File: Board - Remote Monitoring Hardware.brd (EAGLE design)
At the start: 92.7 x 49.8 mm, 49 parts, among them IC1 MSP430G2 Socket, IC2 TPS77301, IC3 Xbee S3 Socket, IC4 MAX31855T, J5 Mono 2.5mm, Q1 MC-405

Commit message: board and schematics update May 25 2017
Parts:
- removed J5: Mono 2.5mm, con-lumberg:1501_05
- added J5A: (no value), SparkFun-Connectors:SCREWTERMINAL-3.5MM-2
- added J5B: PCC-SMP, custom parts:PCC-SMP
- C7: value 1uF/6.3V -> 10uF
- C8: value 100uF -> 100nF
- moved IC4 54.0 mm to (55.2, 35.6), turned to 0 degrees
- moved R8 42.3 mm to (47.0, 37.5), turned to 0 degrees
- moved S3 40.4 mm to (5.71, 12.7), turned to 180 degrees
- moved R9 40.0 mm to (40.0, 37.5), turned to 0 degrees
- moved J7 35.1 mm to (5.08, 25.4), turned to 270 degrees
- moved L1 34.5 mm to (51.4, 23.5)
- moved C9 33.8 mm to (54.0, 26.7), turned to 0 degrees
- moved L2 33.2 mm to (56.5, 23.5)
- moved J2 32.4 mm to (30.5, 20.3)
- moved C11 29.3 mm to (34.9, 37.5), turned to 0 degrees
- moved C10 28.7 mm to (29.8, 37.5), turned to 0 degrees
- moved C1 25.1 mm to (12.7, 4.45), turned to 180 degrees
- moved C2 24.8 mm to (17.8, 4.45), turned to 180 degrees
- moved D2 24.0 mm to (27.9, 3.81)
- moved R4 19.3 mm to (40.0, 20.3)
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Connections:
- removed net DIN: J6.2
- removed net DOUT: J6.3
- net N$14: now also J5A.2, J5B.T-; no longer J5.2, J5.3
- net N$15: now also J5A.1, J5B.T+; no longer J5.1
- net P1.1: now also J6.3
- net P1.2: now also J6.2
- net VCC: now also S2.1; no longer S2.2
- net VCC_XBEE: now also S2.2; no longer S2.1
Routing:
- net VCC: track 0.00 -> 132.9 mm, vias 0 -> 2
- net P1.2: track 0.00 -> 113.9 mm
- net P1.1: track 0.00 -> 110.6 mm
- net VCC_XBEE: track 0.00 -> 110.3 mm
- net 1: track 0.00 -> 109.8 mm, vias 0 -> 2
- net RST/SBWTDIO: track 0.00 -> 94.6 mm, vias 0 -> 2
- net 2: track 0.00 -> 83.2 mm, vias 0 -> 4
- net P1.3: track 0.00 -> 55.7 mm, vias 0 -> 2
- net +3.3VIN1: track 0.00 -> 46.2 mm
- net XOUTR: track 0.00 -> 43.5 mm
- net N$15: track 0.00 -> 41.2 mm
- net P1.6: track 0.00 -> 40.7 mm, vias 0 -> 2
- net N$14: track 0.00 -> 39.6 mm
- net +3.3VIN2: track 0.00 -> 35.8 mm
- net XINR: track 0.00 -> 35.1 mm
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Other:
- board size 92.7 x 49.8 mm -> 92.7 x 56.2 mm
- board text added: "(C) 2017 Vincent Aulia"
- board text added: "MSP430 Target Board Socket Mark I"
- board text removed: "MSP430G2 Target Socket Mark I"

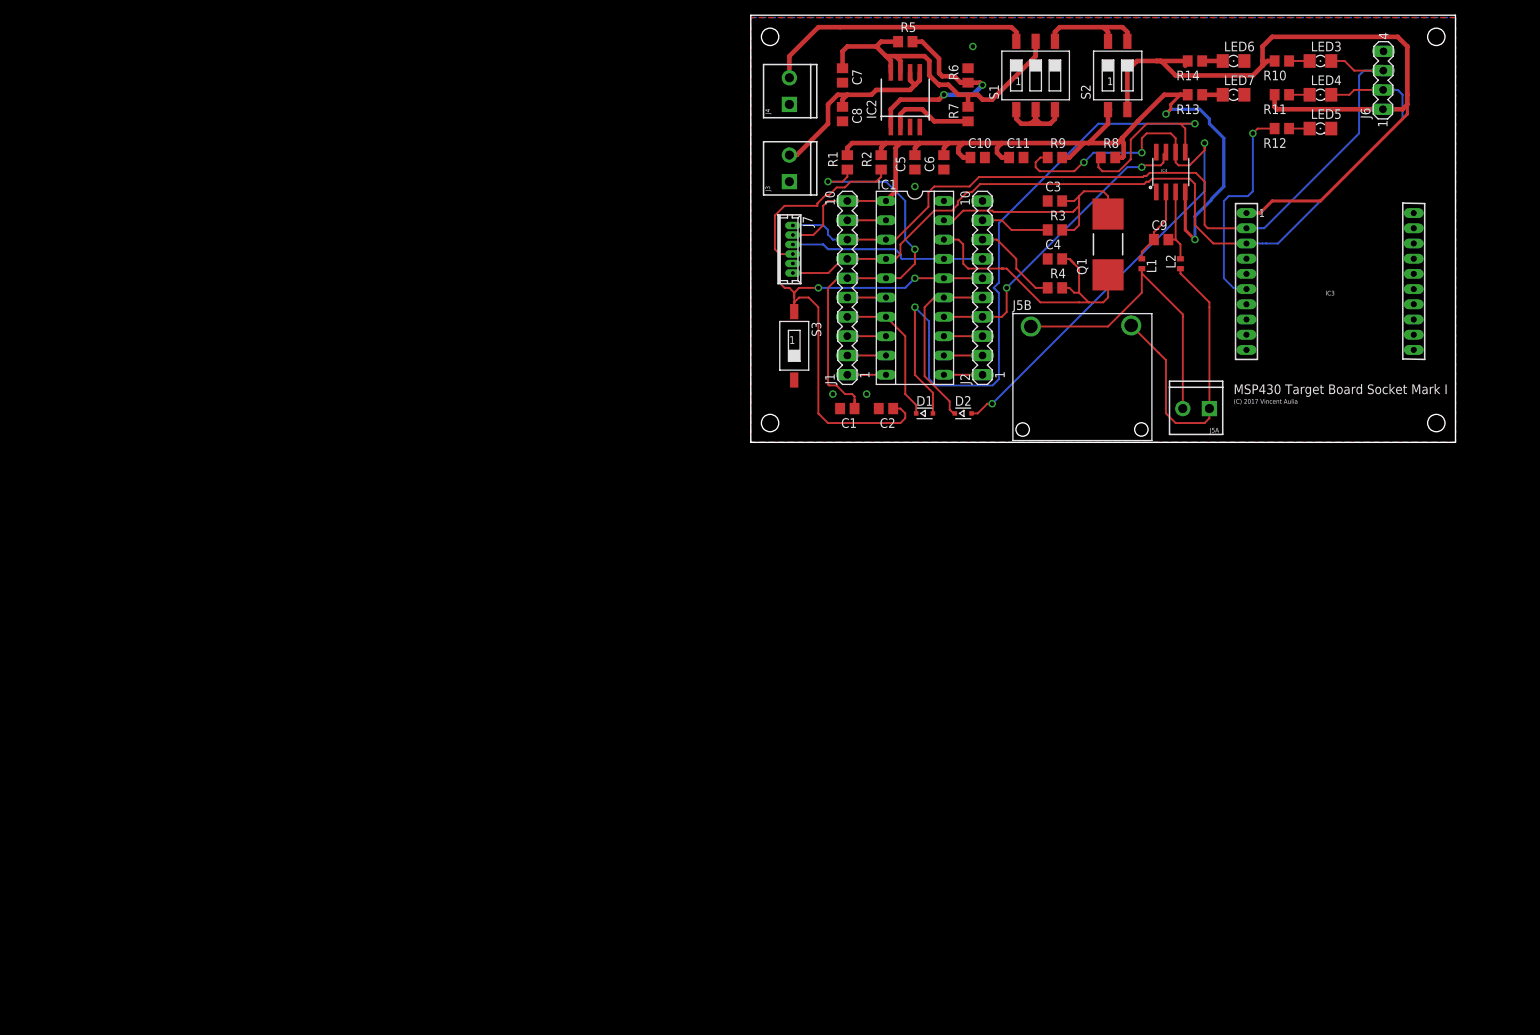
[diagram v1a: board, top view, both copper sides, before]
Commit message: Added BOM + brd & sch changes Aug 28 2017
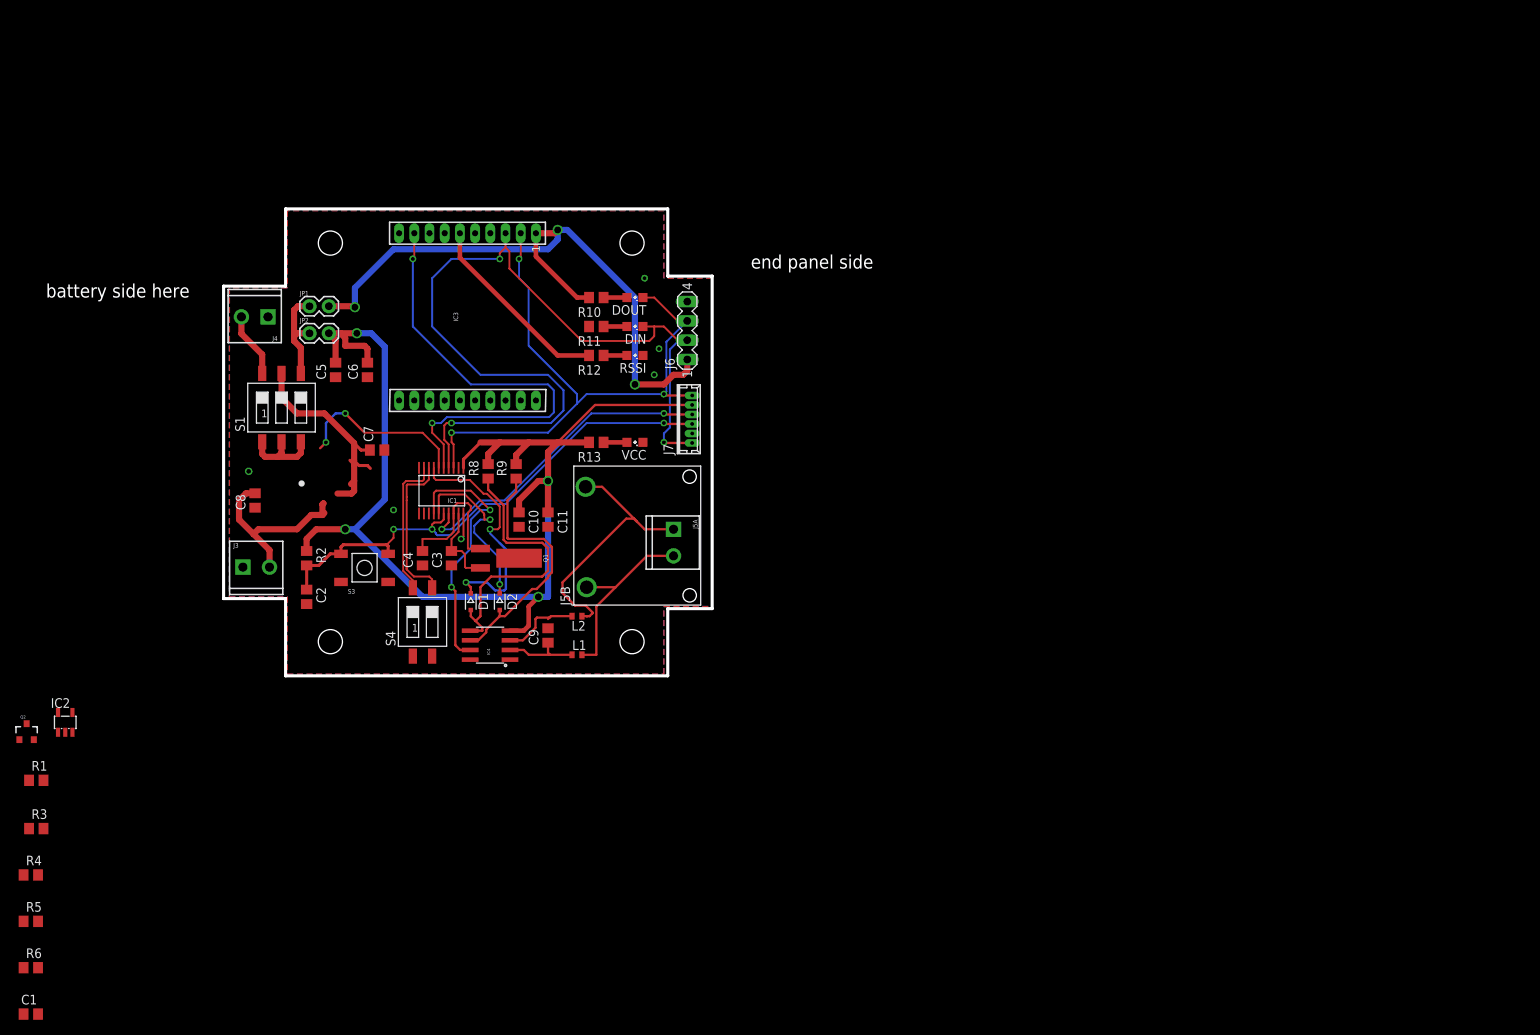
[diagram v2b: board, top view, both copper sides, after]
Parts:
- removed J1, J2: (no value), con-lstb:MA10-1
- removed LED3, LED4, LED6, LED7: Green, eagle-ltspice:LED_1206
- removed LED5: Red, eagle-ltspice:LED_1206
- removed R14: 1k, eagle-ltspice:R0805
- removed R7: 250k, eagle-ltspice:R0805
- removed S2: (no value), smd-special:SMS-002
- added DIN: LED4, led:SML0805
- added DOUT: LED3, led:SML0805
- added JP1, JP2: (no value), SparkFun-Retired:1X02
- added Q2: DMP3099L-7, User-Submitted:SOT23-3
- added RSSI: LED5, led:SML0805
- added S4: (no value), smd-special:SMS-002
- added VCC: LED7, led:SML0805
- C1: value 100nF -> 0.1uF
- C7: value 10uF -> 4.7uF
- C8: value 100nF -> 1uF
- IC1: value MSP430G2 Socket -> MSP430G2553; device ic-package:SOCKET-20 -> custom parts:MSP430G2553IPW20
- IC2: value TPS77301 -> TPS77001; device texas:SOP-08 -> texas:SOT23-DBV
- Q1: value MC-405 -> 32.768kHz; device crystal:MC-405 -> SparkFun-Clocks:CRYSTAL-SMD-2X6-CYL
- R1: value 47k -> 287k
- R3: value 0R -> 169k
- R4: value 0R -> 172k
- R5: value 53.8k -> 100k
- R6: value 30.1k -> 10k
- S3: value (none) -> SMD-PUSHBTN-SWTVER1; device smd-special:SMS-001 -> custom parts:KPT-1187B
- moved R6 170.2 mm to (-94.7, -69.1), turned to 0 degrees
- moved R5 163.1 mm to (-94.7, -63.0)
- moved R3 155.4 mm to (-94.0, -50.8)
- moved R4 155.3 mm to (-94.7, -56.9)
- moved IC2 137.5 mm to (-90.2, -36.8)
- moved R1 134.1 mm to (-94.0, -44.5), turned to 0 degrees
- moved C1 133.7 mm to (-94.7, -75.2), turned to 0 degrees
- moved IC3 124.6 mm to (-48.3, 16.5), turned to 270 degrees
- moved IC4 109.0 mm to (-34.3, -26.7), turned to 90 degrees
- moved S1 108.4 mm to (-61.7, 4.57)
- moved J6 97.3 mm to (-8.36, 14.7), turned to 90 degrees
- moved C9 96.0 mm to (-26.7, -25.4), turned to 90 degrees
- moved R10 95.4 mm to (-20.3, 19.1)
- moved R11 95.2 mm to (-20.3, 15.2)
- moved R12 95.0 mm to (-20.3, 11.4)
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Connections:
- removed net DTR: IC3.9
- removed net N$18: LED6.A, R14.1
- removed net XIN: J2.9, R3.1
- removed net XOUT: J2.8, R4.1
- new net N$3: Q2.3, R4.2
- net +3.3VIN1: now also IC2.5, R1.2; no longer IC2.7, IC2.8, R5.1, R7.2
- net +9VIN: now also IC2.1, Q2.2, R6.2; no longer IC2.5, IC2.6
- net GND: now also IC2.2, R3.1, R5.1, RSSI.C, S3.3, S3.4, S4.1, S4.2, VCC.C; no longer C1.2, IC2.4, J2.10, LED5.C, LED6.C, LED7.C, R6.2, S3.2
- net N$10: now also DIN.A; no longer LED4.A
- net N$11: now also RSSI.A; no longer LED5.A
- net N$16: now also JP1.1, JP2.1; no longer S2.3, S2.4
- net N$17: now also VCC.A; no longer LED7.A
- net N$2: now also C1.2, Q2.1; no longer IC2.1, R5.2
- net N$4: now also DOUT.A; no longer LED3.A
- net N$5: now also IC2.4, R1.1, R3.2; no longer IC2.2, R7.1
- net P1.0: no longer J1.9
- net P1.1: now also DOUT.C; no longer J1.8, LED3.C
- net P1.2: now also DIN.C; no longer J1.7, LED4.C
- net P1.3: now also IC3.9; no longer C1.1, J1.6, R1.1
- net P1.4: now also R4.1, R5.2; no longer J1.5
- net P1.5: no longer J1.4
- net P1.6: no longer J2.4
- net P1.7: no longer J2.5
- net P2.0: now also S4.3; no longer J1.3
- net P2.1: now also S4.4; no longer J1.2
- net P2.2: now also C1.1; no longer J1.1
- net P2.3: no longer J2.1
- net P2.4: no longer J2.2
- net P2.5: no longer J2.3
- net RST/SBWTDIO: now also S3.2; no longer J2.6
- net TEST/SBWTCK: no longer J2.7
- net VCC: now also JP2.2; no longer J1.10, R1.2, S2.1
- net VCC_XBEE: now also JP1.2; no longer R14.2, S2.2
- net XINR: now also Q1.X2; no longer Q1.2, R3.2
- net XOUTR: now also Q1.X1; no longer Q1.1, R4.2
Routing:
- net 1: track 109.8 -> 37.6 mm, vias 2 -> 0
- net 2: track 83.2 -> 33.5 mm, vias 4 -> 0
- net VCC: track 132.9 -> 166.2 mm, vias 2 -> 4
- net N$2: track 28.4 -> 0.00 mm, vias 2 -> 0
- net P1.1: track 110.6 -> 82.3 mm, vias 0 -> 3
- net +3.3VIN2: track 35.8 -> 8.58 mm
- net RST/SBWTDIO: track 94.6 -> 68.1 mm, vias 2 -> 3
- net XINR: track 35.1 -> 11.0 mm
- net VCC_XBEE: track 110.3 -> 86.3 mm, vias 0 -> 3
- net XOUTR: track 43.5 -> 19.7 mm
- net P1.4: track 5.08 -> 23.4 mm, vias 0 -> 2
- net +3.3VIN1: track 46.2 -> 30.2 mm
- net P2.0: track 5.08 -> 21.0 mm
- net TEST/SBWTCK: track 26.0 -> 41.8 mm, vias 0 -> 2
- net N$14: track 39.6 -> 25.0 mm
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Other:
- board size 92.7 x 56.2 mm -> 64.3 x 61.4 mm
- board text added: "battery side here"
- board text added: "end panel side"
- board text removed: "(C) 2017 Vincent Aulia"
- board text removed: "MSP430 Target Board Socket Mark I"

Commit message: brd & sch changes Sept 12 2017
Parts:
- moved C1 86.8 mm to (-46.8, -2.78), turned to 180 degrees
- moved R5 82.1 mm to (-44.0, 1.48), turned to 270 degrees
- moved R6 77.8 mm to (-48.7, -6.33), turned to 180 degrees
- moved R4 75.6 mm to (-46.6, 1.49), turned to 90 degrees
- moved Q2 58.2 mm to (-51.1, -0.14), turned to 270 degrees
- moved R3 57.2 mm to (-57.1, -6.99), turned to 90 degrees
- moved R1 55.7 mm to (-54.6, -5.08), turned to 90 degrees
- moved IC2 42.6 mm to (-61.8, -5.03), turned to 270 degrees
- moved C7 6.65 mm to (-53.7, 3.81)
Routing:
- net N$2: track 0.00 -> 23.6 mm, vias 0 -> 2
- net +9VIN: track 25.2 -> 43.2 mm
- net P1.4: track 23.4 -> 8.63 mm, vias 2 -> 0
- net N$5: track 0.00 -> 5.99 mm
- net N$3: track 0.00 -> 5.86 mm
- net +3.3VIN1: track 30.2 -> 25.0 mm
- net P2.2: track 0.00 -> 4.52 mm
- net VCC_XBEE: track 86.3 -> 90.1 mm
- net N$13: track 10.4 -> 11.6 mm
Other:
- board text added: "3.3V"
- board text added: "9V"
- board text added: "D"
- board text added: "G"
- board text added: "GND"
- board text added: "P1.1"
- board text added: "P1.2"
- board text added: "P1.3"
- board text added: "P1.5"
- board text added: "P1.6"
- board text added: "P1.7"
- board text added: "RST/SBWTDIO"
- board text added: "S"
- board text added: "TEST/SBWTCK"
- board text added: "VCC"
- board text added: "VCC_ XBEE"

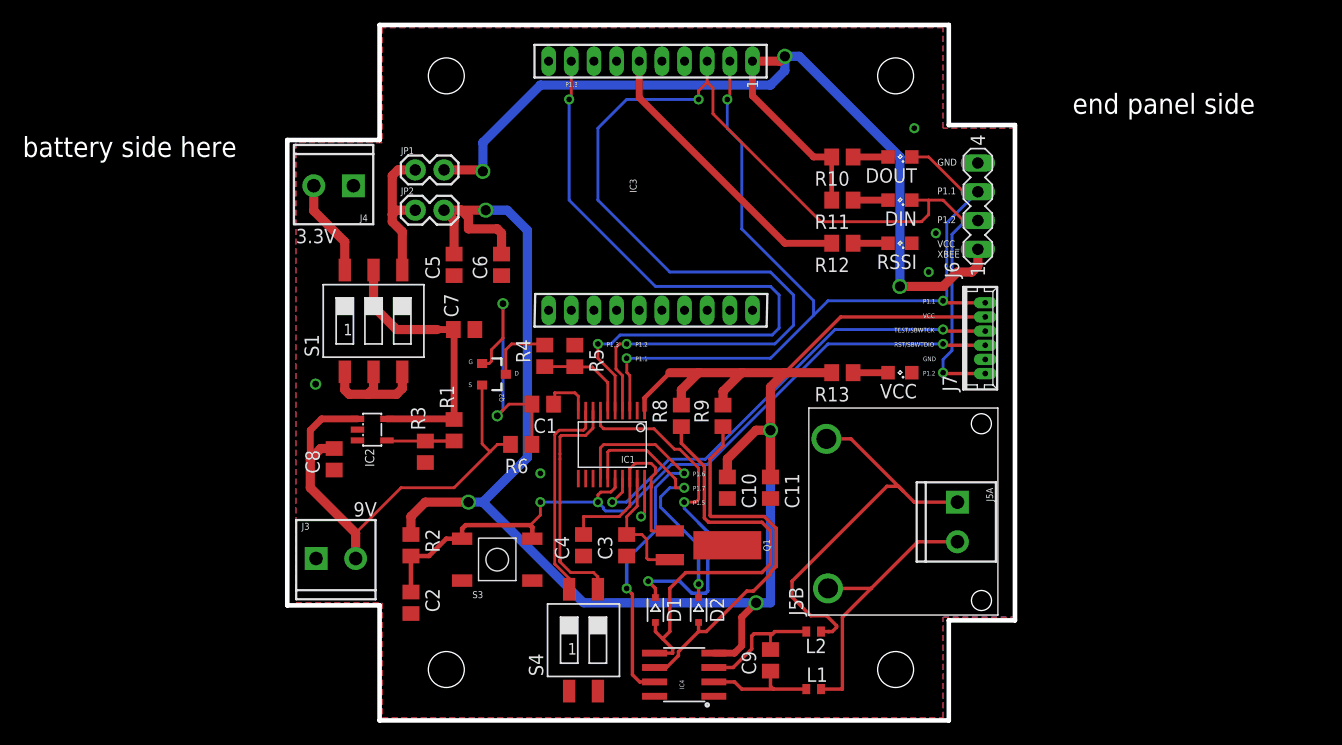
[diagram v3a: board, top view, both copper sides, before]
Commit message: brd sch BOM changes Sept 20 2017
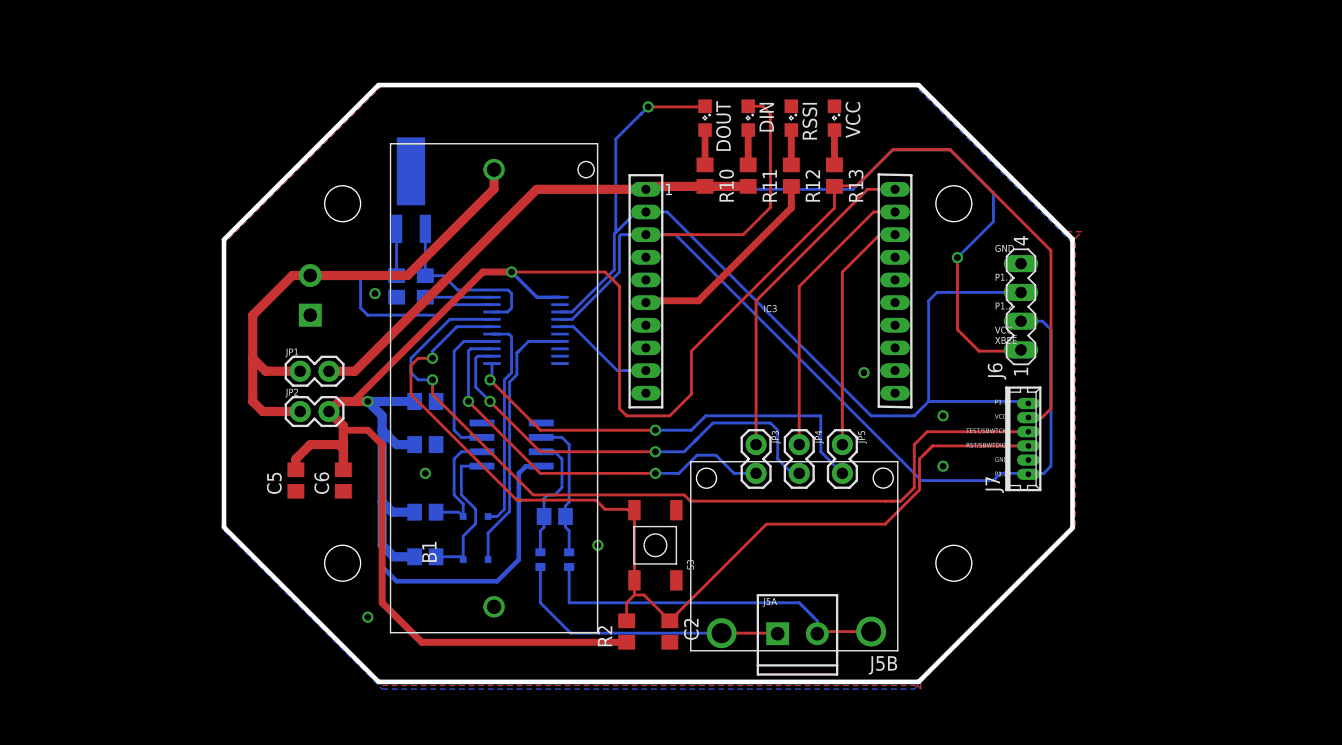
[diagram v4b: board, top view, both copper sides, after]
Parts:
- removed C1: 0.1uF, eagle-ltspice:C0805
- removed C7: 4.7uF, eagle-ltspice:C0805
- removed C8: 1uF, eagle-ltspice:C0805
- removed IC2: TPS77001, texas:SOT23-DBV
- removed J3: (no value), SparkFun-Connectors:SCREWTERMINAL-3.5MM-2
- removed Q2: DMP3099L-7, User-Submitted:SOT23-3
- removed R1: 287k, eagle-ltspice:R0805
- removed R3: 169k, eagle-ltspice:R0805
- removed R4: 172k, eagle-ltspice:R0805
- removed R5: 100k, eagle-ltspice:R0805
- removed R6: 10k, eagle-ltspice:R0805
- removed S1: (no value), smd-special:SMS-003
- removed S4: (no value), smd-special:SMS-002
- added B1: BATT_HLDR_2/3A_THRUHOLE, custom parts:BATT_HLDR_2/3A_THRUHOLE
- added JP3, JP4, JP5: (no value), SparkFun-Retired:1X02
- moved Q1 36.1 mm to (-58.4, 12.7), flipped to the bottom, turned to 0 degrees
- moved C11 30.7 mm to (-57.1, -6.35), flipped to the bottom, turned to 180 degrees
- moved C3 30.6 mm to (-59.7, 7.62), flipped to the bottom
- moved IC3 29.6 mm to (-26.7, -3.81), turned to 0 degrees
- moved C10 27.7 mm to (-57.1, -2.54), flipped to the bottom, turned to 180 degrees
- moved R9 27.6 mm to (-57.1, -12.3), flipped to the bottom, turned to 0 degrees
- moved C4 26.8 mm to (-57.1, 7.62), flipped to the bottom
- moved R8 25.8 mm to (-57.1, -16.3), flipped to the bottom, turned to 0 degrees
- moved IC4 25.4 mm to (-49.5, -6.35), flipped to the bottom, turned to 270 degrees
- moved L2 25.0 mm to (-47.0, -16.5), flipped to the bottom, turned to 90 degrees
- moved L1 24.4 mm to (-44.5, -16.5), flipped to the bottom, turned to 270 degrees
- moved C5 23.6 mm to (-68.6, -9.53)
- moved C6 23.6 mm to (-64.4, -9.53)
- moved VCC 23.2 mm to (-21.0, 22.5), turned to 270 degrees
- moved C2 23.0 mm to (-35.6, -22.9)
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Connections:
- removed net +3.3VIN1: C7.2, IC2.5, R1.2, S1.5
- removed net +3.3VIN2: J4.2, S1.6
- removed net +9VIN: C8.2, IC2.1, J3.2, Q2.2, R6.2
- removed net N$16: JP1.1, JP2.1, S1.4
- removed net N$2: C1.2, Q2.1, R6.1
- removed net N$3: Q2.3, R4.2
- removed net N$5: IC2.4, R1.1, R3.2
- net DIO0: now also JP3.1
- net DIO1: now also JP4.1
- net DIO2: now also JP5.1
- net GND: now also B1.NEG; no longer C7.1, C8.1, IC2.2, IC2.3, J3.1, R3.1, R5.1, S4.1, S4.2
- net N$1: now also B1.POS, J4.2, JP1.1, JP2.1; no longer S1.1, S1.2, S1.3
- net P1.4: no longer R4.1, R5.2
- net P2.0: no longer S4.3
- net P2.1: no longer S4.4
- net P2.2: no longer C1.1
- net P2.3: now also JP5.2
- net P2.4: now also JP4.2
- net P2.5: now also JP3.2
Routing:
- net VCC: track 166.2 -> 224.8 mm, vias 4 -> 2
- net P1.3: track 60.4 -> 9.19 mm, vias 2 -> 0
- net +9VIN: track 43.2 -> 0.00 mm
- net P2.4: track 0.00 -> 39.8 mm, vias 0 -> 2
- net P2.3: track 0.00 -> 39.0 mm, vias 0 -> 2
- net P2.5: track 0.00 -> 36.0 mm, vias 0 -> 2
- net N$1: track 10.7 -> 44.5 mm
- net TEST/SBWTCK: track 41.8 -> 74.6 mm, vias 2 -> 1
- net DIO0: track 0.00 -> 30.2 mm
- net DIO1: track 0.00 -> 25.2 mm
- net +3.3VIN1: track 25.0 -> 0.00 mm
- net 1: track 37.6 -> 13.6 mm
- net N$2: track 23.6 -> 0.00 mm, vias 2 -> 0
- net P1.2: track 118.9 -> 95.5 mm, vias 3 -> 0
- net 2: track 33.5 -> 10.7 mm
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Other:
- board size 64.3 x 61.4 mm -> 74.9 x 52.7 mm
- board text removed: "3.3V"
- board text removed: "9V"
- board text removed: "D"
- board text removed: "G"
- board text removed: "P1.3"
- board text removed: "P1.6"
- board text removed: "P1.7"
- board text removed: "S"
- board text removed: "battery side here"
- board text removed: "end panel side"
